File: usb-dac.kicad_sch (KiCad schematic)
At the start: 28 parts, among them J1 AudioJack3, P1 USB_C_Plug_USB2.0, U1 PCM2912APJTR, Y1 6 Mhz

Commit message: Work on PCB
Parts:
- J1: footprint (none) -> Connector_Audio:Jack_3.5mm_CUI_SJ1-3523N_Horizontal
- P1: footprint (none) -> Connector_USB:USB_C_Receptacle_GCT_USB4105-xx-A_16P_TopMnt_Horizontal
- U1: footprint PJT32 -> Package_QFP:TQFP-32_7x7mm_P0.8mm
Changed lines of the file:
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@@
 			)
 		)
-		(property "Footprint" ""
+		(property "Footprint" "Connector_USB:USB_C_Receptacle_GCT_USB4105-xx-A_16P_TopMnt_Horizontal"
 			(at 33.02 40.64 0)
 			(effects
@@
 			)
 		)
-		(property "Footprint" ""
+		(property "Footprint" "Connector_Audio:Jack_3.5mm_CUI_SJ1-3523N_Horizontal"
 			(at 271.78 120.65 0)
 			(effects
@@
 			)
 		)
-		(property "Footprint" "PJT32"
+		(property "Footprint" "Package_QFP:TQFP-32_7x7mm_P0.8mm"
 			(at 132.08 76.2 0)
 			(effects

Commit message: Add more footprints
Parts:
- R1, R2, R3, R4, R5, R6, R7, R8, R9: footprint (none) -> Resistor_THT:R_Axial_DIN0207_L6.3mm_D2.5mm_P10.16mm_Horizontal
- Y1: value 6 Mhz -> 6 MHz; footprint (none) -> Crystal:Crystal_HC49-U_Vertical
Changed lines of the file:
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@@
 			)
 		)
-		(property "Footprint" ""
+		(property "Footprint" "Resistor_THT:R_Axial_DIN0207_L6.3mm_D2.5mm_P10.16mm_Horizontal"
 			(at 48.514 37.084 90)
 			(effects
@@
 			)
 		)
-		(property "Footprint" ""
+		(property "Footprint" "Resistor_THT:R_Axial_DIN0207_L6.3mm_D2.5mm_P10.16mm_Horizontal"
 			(at 248.666 113.284 90)
 			(effects
@@
 			)
 		)
-		(property "Footprint" ""
+		(property "Footprint" "Resistor_THT:R_Axial_DIN0207_L6.3mm_D2.5mm_P10.16mm_Horizontal"
 			(at 229.616 113.284 90)
 			(effects
@@
 			)
 		)
-		(property "Value" "6 Mhz"
+		(property "Value" "6 MHz"
 			(at 40.386 92.456 90)
 			(effects
@@
 			)
 		)
-		(property "Footprint" ""
+		(property "Footprint" "Crystal:Crystal_HC49-U_Vertical"
 			(at 36.83 91.44 0)
 			(effects
@@
 			)
 		)
-		(property "Footprint" ""
+		(property "Footprint" "Resistor_THT:R_Axial_DIN0207_L6.3mm_D2.5mm_P10.16mm_Horizontal"
 			(at 48.514 29.464 90)
 			(effects
@@
 			)
 		)
-		(property "Footprint" ""
+		(property "Footprint" "Resistor_THT:R_Axial_DIN0207_L6.3mm_D2.5mm_P10.16mm_Horizontal"
 			(at 248.666 132.334 90)
 			(effects
@@
 			)
 		)
-		(property "Footprint" ""
+		(property "Footprint" "Resistor_THT:R_Axial_DIN0207_L6.3mm_D2.5mm_P10.16mm_Horizontal"
 			(at 48.514 48.514 90)
 			(effects
@@
 			)
 		)
-		(property "Footprint" ""
+		(property "Footprint" "Resistor_THT:R_Axial_DIN0207_L6.3mm_D2.5mm_P10.16mm_Horizontal"
 			(at 27.686 91.694 90)
 			(effects
@@
 			)
 		)
-		(property "Footprint" ""
+		(property "Footprint" "Resistor_THT:R_Axial_DIN0207_L6.3mm_D2.5mm_P10.16mm_Horizontal"
 			(at 48.514 42.164 90)
 			(effects
@@
 			)
 		)
-		(property "Footprint" ""
+		(property "Footprint" "Resistor_THT:R_Axial_DIN0207_L6.3mm_D2.5mm_P10.16mm_Horizontal"
 			(at 229.616 132.334 90)
 			(effects

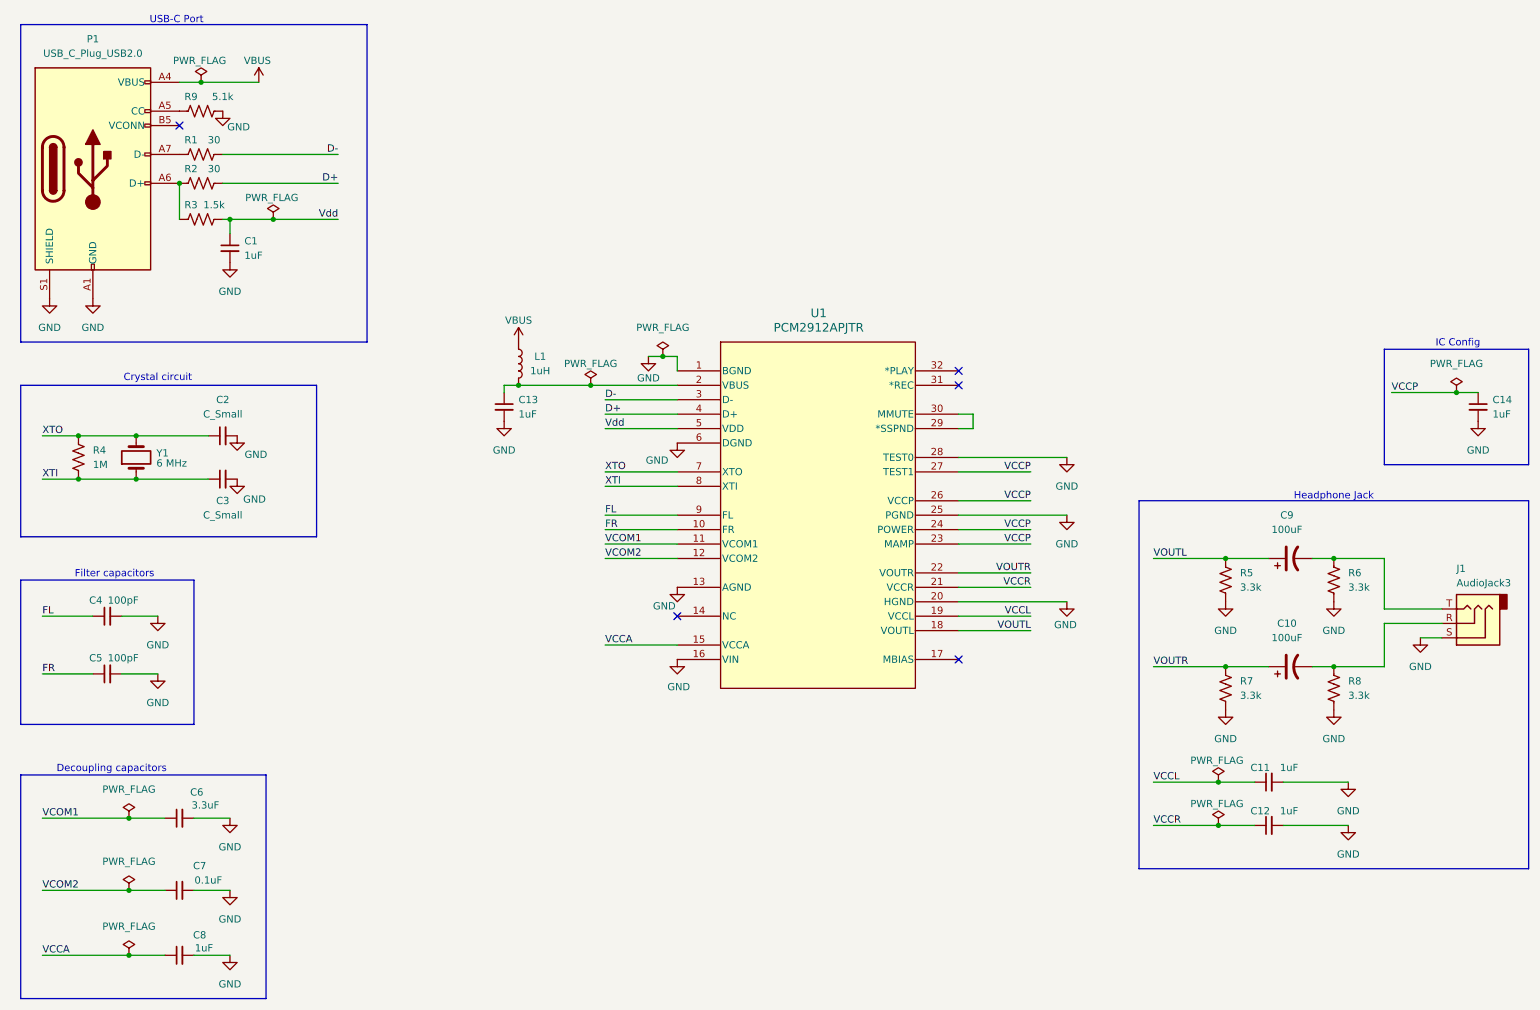
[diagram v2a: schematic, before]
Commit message: BOM edits and footprint additions
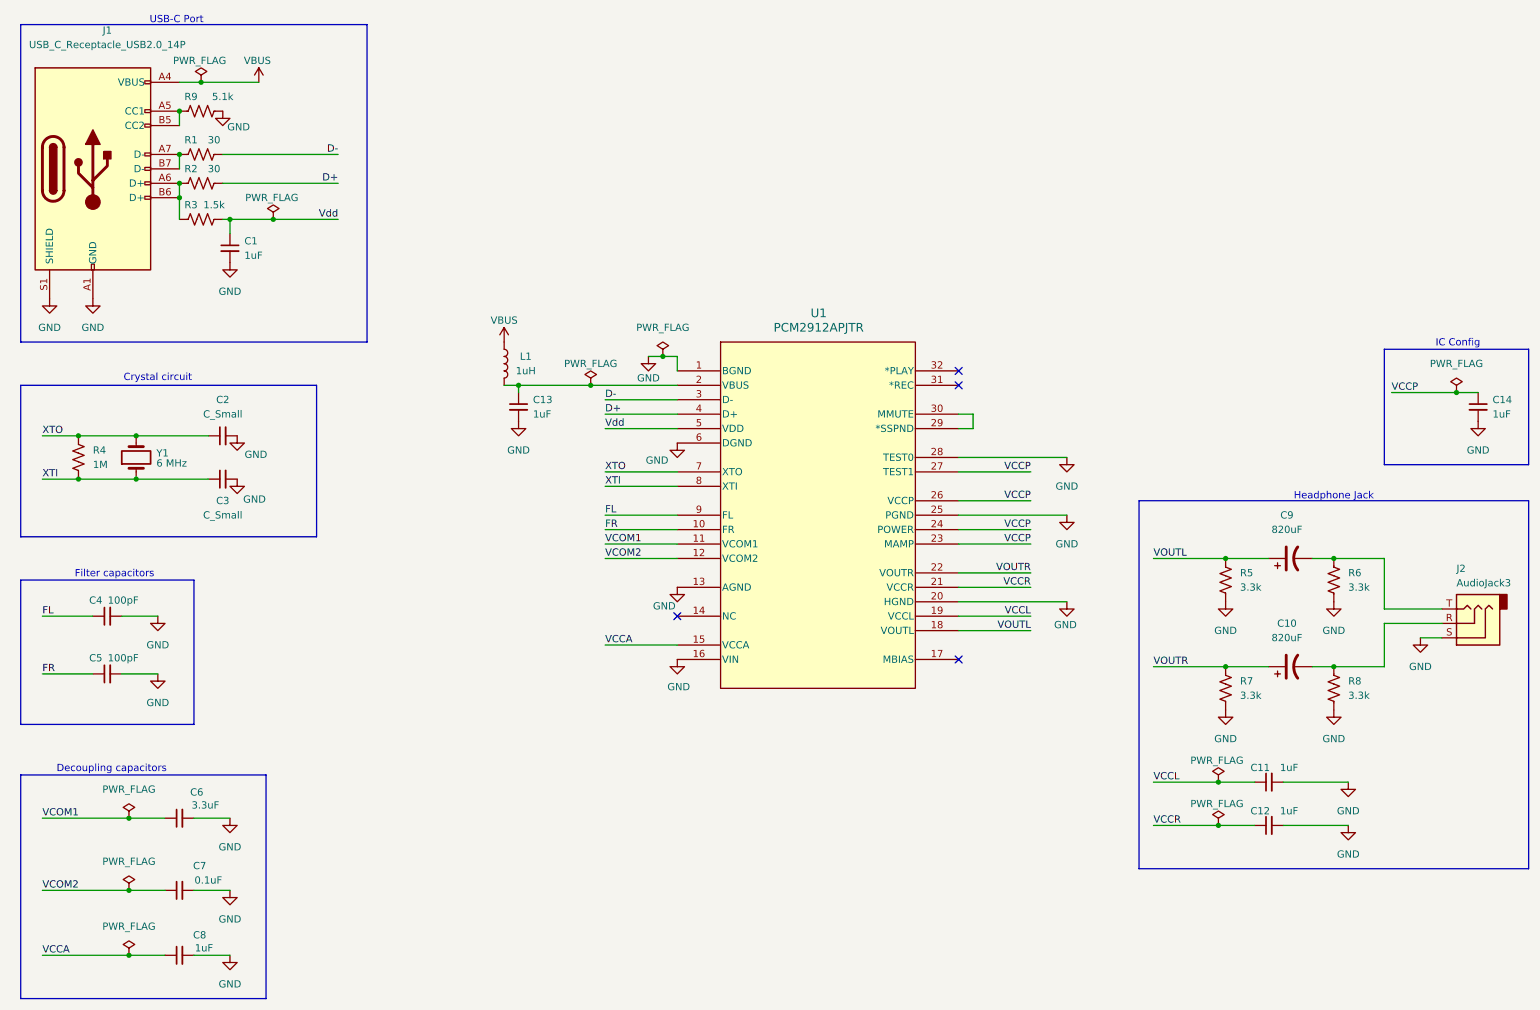
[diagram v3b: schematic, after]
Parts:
- removed P1: USB_C_Plug_USB2.0, Connector_USB:USB_C_Receptacle_GCT_USB4105-xx-A_16P_TopMnt_Horizontal, symbol Connector:USB_C_Plug_USB2.0
- added J1: USB_C_Receptacle_USB2.0_14P, Connector_USB:USB_C_Receptacle_GCT_USB4085, symbol Connector:USB_C_Receptacle_USB2.0_14P
- C1, C11, C12, C13, C14, C8: footprint (none) -> Capacitor_THT:C_Rect_L7.0mm_W2.0mm_P5.00mm; Mfr. # (none) -> FG28X7R1E105KRT00
- C10, C9: value 100uF -> 820uF; footprint (none) -> Capacitor_THT:CP_Radial_D8.0mm_P3.50mm; Mfr. # (none) -> 6.3ZLH820MEFC8X11.5
- J2: renamed from J1; Mfr. # (none) -> SJ1-3523N
- L1: footprint (none) -> Inductor_THT:L_Axial_L5.3mm_D2.2mm_P7.62mm_Horizontal_Vishay_IM-1; Mfr. # (none) -> AICC-02-1R0M-T
- U1: Mfr. # (none) -> PCM2912APJTR
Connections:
- net GND: now also J1.A1 (GND), J1.A12 (GND), J1.B1 (GND), J1.B12 (GND), J1.S1 (SHIELD)
- net VBUS: now also J1.A4 (VBUS), J1.A9 (VBUS), J1.B4 (VBUS), J1.B9 (VBUS)
- net at R1.1: now also J1.A7 (D-), J1.B7 (D-)
- net at R9.1: now also J1.A5 (CC1), J1.B5 (CC2)
- net at R2.1, R3.1: now also J1.A6 (D+), J1.B6 (D+)
- no-connect marks 5 -> 4
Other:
- moved on the sheet: C13, L1

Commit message: BOM and footprint work
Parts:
- C1, C11, C12, C13, C14, C8: Mfr. (none) -> TDK
- C10, C9: Mfr. (none) -> Rubycon
- C2, C3: value C_Small -> 30pF; Mfr. (none) -> Vishay; Mfr. # (none) -> K300J10C0GF5UH5
- J1: Mfr. (none) -> GCT
- J2: Mfr. (none) -> CUI Devices
- L1: Mfr. (none) -> ABRACON
- R1, R2: Mfr. (none) -> SEI Stackpole; Mfr. # (none) -> CF14JT30R0
- R3: Mfr. (none) -> YAGEO; Mfr. # (none) -> CFR-12JB-52-1K5
- R4: Mfr. (none) -> SEI Stackpole; Mfr. # (none) -> RNF18FTD1M00
- R5, R6, R7, R8: Mfr. (none) -> SEI Stackpole; Mfr. # (none) -> CFM14JT3K30
- R9: Mfr. (none) -> SEI Stackpole; Mfr. # (none) -> CF18JT5K10
- U1: Mfr. (none) -> Texas Instruments
- Y1: Mfr. (none) -> CTS Electronic Components; Mfr. # (none) -> ATS060

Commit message: Start PCB placements
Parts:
- C2, C3: footprint (none) -> Capacitor_THT:C_Rect_L7.0mm_W2.0mm_P5.00mm
- C4, C5: footprint (none) -> Capacitor_THT:C_Rect_L7.0mm_W2.0mm_P5.00mm; Mfr. (none) -> Walsin; Mfr. # (none) -> XR501101K040HAND5P
- C6: footprint (none) -> Capacitor_THT:C_Rect_L7.0mm_W2.0mm_P5.00mm; Mfr. (none) -> TDK; Mfr. # (none) -> FA24X7R1E335KRU06
- C7: footprint (none) -> Capacitor_THT:C_Rect_L7.0mm_W2.0mm_P5.00mm; Mfr. (none) -> Vishay; Mfr. # (none) -> K104K10X7RF5UH5
- J1: footprint Connector_USB:USB_C_Receptacle_GCT_USB4085 -> Connector_USB:USB_C_Receptacle_GCT_USB4105-xx-A_16P_TopMnt_Horizontal
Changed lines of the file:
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@@
 			)
 		)
-		(property "Footprint" ""
+		(property "Footprint" "Capacitor_THT:C_Rect_L7.0mm_W2.0mm_P5.00mm"
 			(at 31.75 119.38 0)
 			(effects
@@
 			)
 		)
-		(property "Mfr. #" ""
+		(property "Mfr. #" "XR501101K040HAND5P"
 			(at 31.75 119.38 0)
 			(effects
@@
 			)
 		)
-		(property "Mfr." ""
+		(property "Mfr." "Walsin"
 			(at 31.75 119.38 0)
 			(effects
@@
 			)
 		)
-		(property "Footprint" ""
+		(property "Footprint" "Capacitor_THT:C_Rect_L7.0mm_W2.0mm_P5.00mm"
 			(at 31.75 129.54 0)
 			(effects
@@
 			)
 		)
-		(property "Mfr. #" ""
+		(property "Mfr. #" "XR501101K040HAND5P"
 			(at 31.75 129.54 0)
 			(effects
@@
 			)
 		)
-		(property "Mfr." ""
+		(property "Mfr." "Walsin"
 			(at 31.75 129.54 0)
 			(effects
@@
 			)
 		)
-		(property "Footprint" ""
+		(property "Footprint" "Capacitor_THT:C_Rect_L7.0mm_W2.0mm_P5.00mm"
 			(at 52.07 87.63 0)
 			(effects
@@
 			)
 		)
-		(property "Footprint" ""
+		(property "Footprint" "Capacitor_THT:C_Rect_L7.0mm_W2.0mm_P5.00mm"
 			(at 52.07 95.25 0)
 			(effects
@@
 			)
 		)
-		(property "Footprint" "Connector_USB:USB_C_Receptacle_GCT_USB4085"
+		(property "Footprint" "Connector_USB:USB_C_Receptacle_GCT_USB4105-xx-A_16P_TopMnt_Horizontal"
 			(at 33.02 40.64 0)
 			(effects
@@
 			)
 		)
-		(property "Footprint" ""
+		(property "Footprint" "Capacitor_THT:C_Rect_L7.0mm_W2.0mm_P5.00mm"
 			(at 44.45 154.94 0)
 			(effects
@@
 			)
 		)
-		(property "Mfr. #" ""
+		(property "Mfr. #" "FA24X7R1E335KRU06"
 			(at 44.45 154.94 0)
 			(effects
@@
 			)
 		)
-		(property "Mfr." ""
+		(property "Mfr." "TDK"
 			(at 44.45 154.94 0)
 			(effects
@@
 			)
 		)
-		(property "Footprint" ""
+		(property "Footprint" "Capacitor_THT:C_Rect_L7.0mm_W2.0mm_P5.00mm"
 			(at 44.45 167.64 0)
 			(effects
@@
 			)
 		)
-		(property "Mfr. #" ""
+		(property "Mfr. #" "K104K10X7RF5UH5"
 			(at 44.45 167.64 0)
 			(effects
@@
 			)
 		)
-		(property "Mfr." ""
+		(property "Mfr." "Vishay"
 			(at 44.45 167.64 0)
 			(effects

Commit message: correct resistor and type-c port models
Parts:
- J1: Mfr. # USB4085 -> USB4105
- R1, R2: Mfr. SEI Stackpole -> YAGEO; Mfr. # CF14JT30R0 -> CFR-12JB-52-30R
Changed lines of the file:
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@@
 			)
 		)
-		(property "Mfr. #" "CF14JT30R0"
+		(property "Mfr. #" "CFR-12JB-52-30R"
 			(at 48.26 38.1 0)
 			(effects
@@
 			)
 		)
-		(property "Mfr." "SEI Stackpole"
+		(property "Mfr." "YAGEO"
 			(at 48.26 38.1 0)
 			(effects
@@
 			)
 		)
-		(property "Mfr. #" "USB4085"
+		(property "Mfr. #" "USB4105"
 			(at 29.21 40.64 0)
 			(effects
@@
 			)
 		)
-		(property "Mfr. #" "CF14JT30R0"
+		(property "Mfr. #" "CFR-12JB-52-30R"
 			(at 48.26 43.18 0)
 			(effects
@@
 			)
 		)
-		(property "Mfr." "SEI Stackpole"
+		(property "Mfr." "YAGEO"
 			(at 48.26 43.18 0)
 			(effects

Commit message: Add a in-stock capacitor part
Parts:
- C2, C3: value 30pF -> 27pF; Mfr. # K300J10C0GF5UH5 -> K270J15C0GF5TH5
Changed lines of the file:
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@@
 			)
 		)
-		(property "Value" "30pF"
+		(property "Value" "27pF"
 			(at 52.0763 83.82 90)
 			(effects
@@
 			)
 		)
-		(property "Mfr. #" "K300J10C0GF5UH5"
+		(property "Mfr. #" "K270J15C0GF5TH5"
 			(at 52.07 87.63 0)
 			(effects
@@
 			)
 		)
-		(property "Value" "30pF"
+		(property "Value" "27pF"
 			(at 52.07 101.6 90)
 			(effects
@@
 			)
 		)
-		(property "Mfr. #" "K300J10C0GF5UH5"
+		(property "Mfr. #" "K270J15C0GF5TH5"
 			(at 52.07 95.25 0)
 			(effects
